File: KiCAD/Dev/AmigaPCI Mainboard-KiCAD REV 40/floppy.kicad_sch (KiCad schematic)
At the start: 24 parts, among them CN203 DB25_Stack_FemaleAndMale, CN204 INTERNAL FLOPPY, J200 SHORT FOR DF1, J201 1-2 AMIGA DRIVES/2-3 PC DRIVES, J202 1-2 AMIGA DRIVES/2-3 PC DRIVES, J207 TICK, J208 TBASE, U204 8520, U209 74HCT08, U212 74HCT74, U213 74HCT00, U215 74HCT03, U305 74HCT08

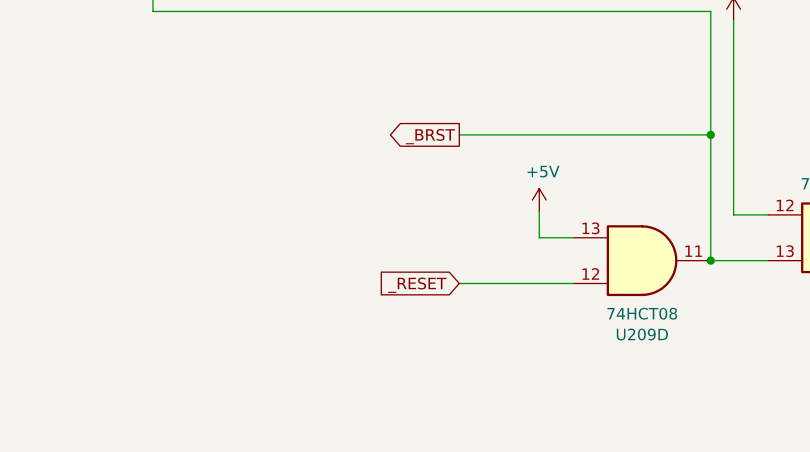
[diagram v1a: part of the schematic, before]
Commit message: AmigaPCI Rev 4.0 Schematic Updates 17-JUL-2024
Changed reset circuit, added _DSACKx, Dropped _LOCKE from Local Bus Port,  added CPU Reset In to Local Bus Port.
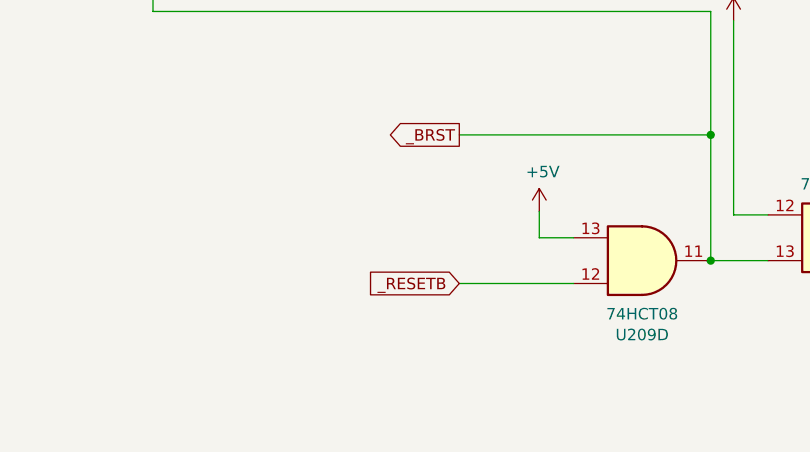
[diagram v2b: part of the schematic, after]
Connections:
- net _RESET renamed _RESETB
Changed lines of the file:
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@@
 	(title_block
 		(title "AMIGA PCI")
-		(date "2024-07-09")
+		(date "2024-07-17")
 		(rev "4.0")
 	)
@@
 		)
 	)
-	(global_label "_RESET"
+	(global_label "_RESETB"
 		(shape input)
 		(at 65.532 243.586 180)
@@
 		)
 		(property "Intersheetrefs" "${INTERSHEET_REFS}"
-			(at 55.9135 243.586 0)
+			(at 54.5641 243.586 0)
 			(effects
 				(font

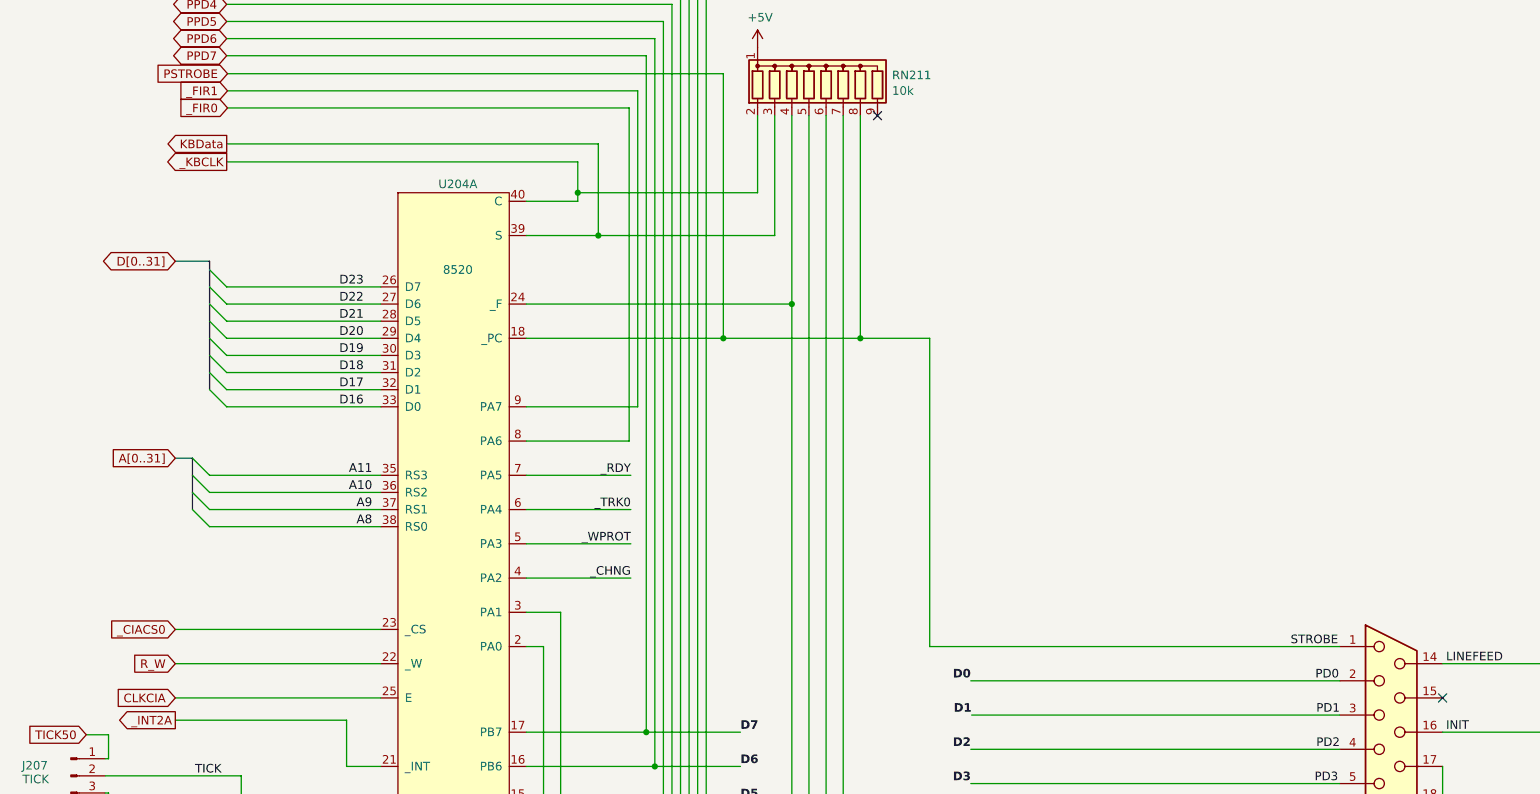
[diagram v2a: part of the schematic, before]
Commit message: AmigaPCI Rev 4.0 Routing
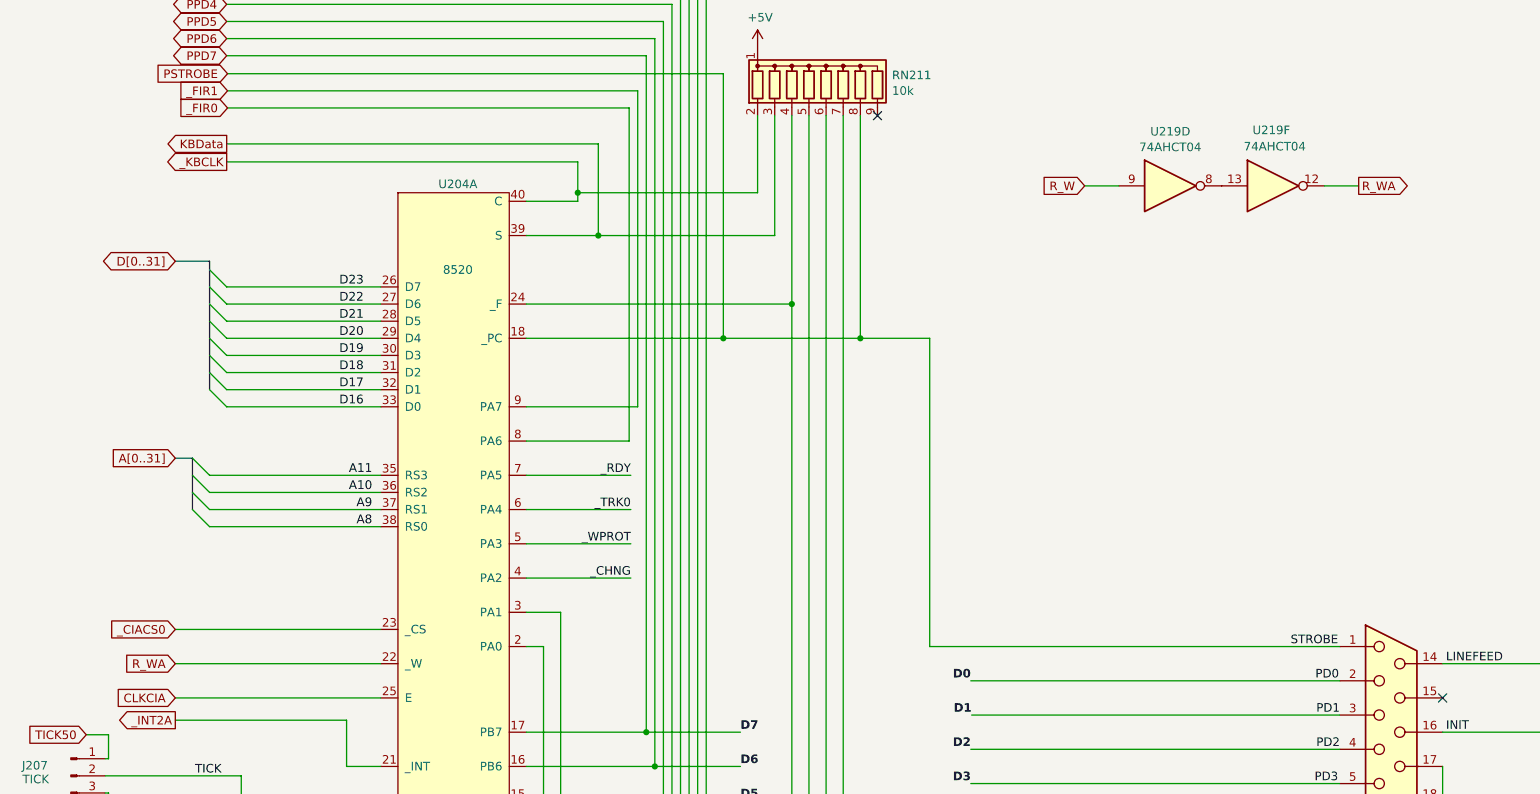
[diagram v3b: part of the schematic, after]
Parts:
- added U219: 74AHCT04, Package_SO:TSSOP-14_4.4x5mm_P0.65mm, symbol 74xx:74LS04
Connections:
- net R_W: now also U219.9; no longer U204.22 (_W)
- new net: U219.13, U219.8
- new net R_WA: U204.22 (_W), U219.12
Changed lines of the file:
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@@
 	(wire
 		(pts
+			(xy 213.36 55.88) (xy 208.28 55.88)
+		)
+		(stroke
+			(width 0)
+			(type default)
+		)
+	)
+	(wire
+		(pts
 			(xy 391.795 221.107) (xy 391.795 216.027)
 		)
@@
 	(wire
 		(pts
+			(xy 172.72 55.88) (xy 177.8 55.88)
+		)
+		(stroke
+			(width 0)
+			(type default)
+		)
+	)
+	(wire
+		(pts
 			(xy 89.916 63.246) (xy 100.584 63.246)
 		)
@@
 		)
 	)
+	(global_label "R_WA"
+		(shape output)
+		(at 213.36 55.88 0)
+		(effects
+			(font
+				(size 1.27 1.27)
+			)
+			(justify left)
+		)
+		(property "Intersheetrefs" "${INTERSHEET_REFS}"
+			(at 221.488 56.134 0)
+			(effects
+				(font
+					(size 1.27 1.27)
+				)
+				(justify left)
+			)
+		)
+	)
 	(global_label "_SIDE"
 		(shape input)
@@
 		)
 	)
+	(global_label "R_W"
+		(shape input)
+		(at 172.72 55.88 180)
+		(effects
+			(font
+				(size 1.27 1.27)
+			)
+			(justify right)
+		)
+		(property "Intersheetrefs" "${INTERSHEET_REFS}"
+			(at 166.624 55.88 0)
+			(effects
+				(font
+					(size 1.27 1.27)
+				)
+				(justify right)
+			)
+		)
+	)
 	(global_label "PPD6"
 		(shape bidirectional)
@@
 		)
 	)
-	(global_label "R_W"
+	(global_label "R_WA"
 		(shape input)
 		(at 37.846 126.746 180)
@@
 	)
 	(symbol
+		(lib_id "74xx:74LS04")
+		(at 185.42 55.88 0)
+		(unit 4)
+		(exclude_from_sim no)
+		(in_bom yes)
+		(on_board yes)
+		(dnp no)
+		(property "Reference" "U219"
+			(at 185.42 47.8282 0)
+			(effects
+				(font
+					(size 1.27 1.27)
+				)
+			)
+		)
+		(property "Value" "74AHCT04"
+			(at 185.42 50.1396 0)
+			(effects
+				(font
+					(size 1.27 1.27)
+				)
+			)
+		)
+		(property "Footprint" "Package_SO:TSSOP-14_4.4x5mm_P0.65mm"
+			(at 185.42 55.88 0)
+			(effects
+				(font
+					(size 1.27 1.27)
+				)
+				(hide yes)
+			)
+		)
+		(property "Datasheet" "http://www.ti.com/lit/gpn/sn74LS04"
+			(at 185.42 55.88 0)
+			(effects
+				(font
+					(size 1.27 1.27)
+				)
+				(hide yes)
+			)
+		)
+		(property "Description" ""
+			(at 185.42 55.88 0)
+			(effects
+				(font
+					(size 1.27 1.27)
+				)
+				(hide yes)
+			)
+		)
+		(pin "1"
+		)
+		(pin "2"
+		)
+		(pin "3"
+		)
+		(pin "4"
+		)
+		(pin "5"
+		)
+		(pin "6"
+		)
+		(pin "8"
+		)
+		(pin "9"
+		)
+		(pin "10"
+		)
+		(pin "11"
+		)
+		(pin "12"
+		)
+		(pin "13"
+		)
+		(pin "14"
+		)
+		(pin "7"
+		)
+		(instances
+			(project "AmigaPCI Mainboard"
+				(path "/72453515-27fe-4336-91f3-e3c8054f7767/64185471-b9ae-4a50-a046-7157e86a04d0"
+					(reference "U219")
+					(unit 4)
+				)
+			)
+		)
+	)
+	(symbol
 		(lib_id "74xx:74LS08")
 		(at 85.852 241.046 0)
@@
 				)
 			)
+		)
+	)
+	(symbol
+		(lib_id "74xx:74LS04")
+		(at 200.66 55.88 0)
+		(unit 6)
+		(exclude_from_sim no)
+		(in_bom yes)
+		(on_board yes)
+		(dnp no)
+		(property "Reference" "U219"
+			(at 200.406 47.625 0)
+			(effects
+				(font
+					(size 1.27 1.27)
+				)
+			)
+		)
+		(property "Value" "74AHCT04"
+			(at 200.914 50.038 0)
+			(effects
+				(font
+					(size 1.27 1.27)
+				)
+			)
+		)
+		(property "Footprint" "Package_SO:TSSOP-14_4.4x5mm_P0.65mm"
+			(at 200.66 55.88 0)
+			(effects
+				(font
+					(size 1.27 1.27)
+				)
+				(hide yes)
+			)
+		)
+		(property "Datasheet" "http://www.ti.com/lit/gpn/sn74LS04"
+			(at 200.66 55.88 0)
+			(effects
+				(font
+					(size 1.27 1.27)
+				)
+				(hide yes)
+			)
+		)
+		(property "Description" ""
+			(at 200.66 55.88 0)
+			(effects
+				(font
+					(size 1.27 1.27)
+				)
+				(hide yes)
+			)
+		)
+		(pin "1"
+		)
+		(pin "2"
+		)
+		(pin "3"
+		)
+		(pin "4"
+		)
+		(pin "5"
+		)
+		(pin "6"
+		)
+		(pin "8"
+		)
+		(pin "9"
+		)
+		(pin "10"
+		)
+		(pin "11"
+		)
+		(pin "12"
+		)
+		(pin "13"
+		)
+		(pin "14"
+		)
+		(pin "7"
+		)
+		(instances
+			(project "AmigaPCI Mainboard"
+				(path "/72453515-27fe-4336-91f3-e3c8054f7767/64185471-b9ae-4a50-a046-7157e86a04d0"
+					(reference "U219")
+					(unit 6)
+				)
+			)
